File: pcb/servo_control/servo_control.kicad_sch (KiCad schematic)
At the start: 53 parts, among them J1 Jack-DC, J10 Conn_01x03_Female, J11 Conn_01x03_Female, J12 Conn_01x03_Female, J13 Conn_01x03_Female, J14 Conn_01x03_Female, J15 Conn_01x03_Female, J16 Conn_01x03_Female, J17 Conn_01x03_Female, J18 Conn_01x03_Female, J19 Conn_01x03_Female, J2 YLIDAR X4, J20 Conn_01x03_Female, J21 Conn_01x06_Male, J22 GY-87, J3 Conn_01x03_Female, J4 Conn_01x03_Female, J5 Conn_01x03_Female, J6 Conn_01x03_Female, J7 Conn_01x03_Female, J8 Conn_01x03_Female, J9 Conn_01x03_Female, SW1 ESP_PROG, SW2 ESP_RST, U1 PCA9685BS, U2 LM317-3.3_SOT-223, U3 ESP32-WROOM-32, U4 MCP73213-A6SI/MF, U5 PCA9685BS, U6 LM317-5_SOT-223

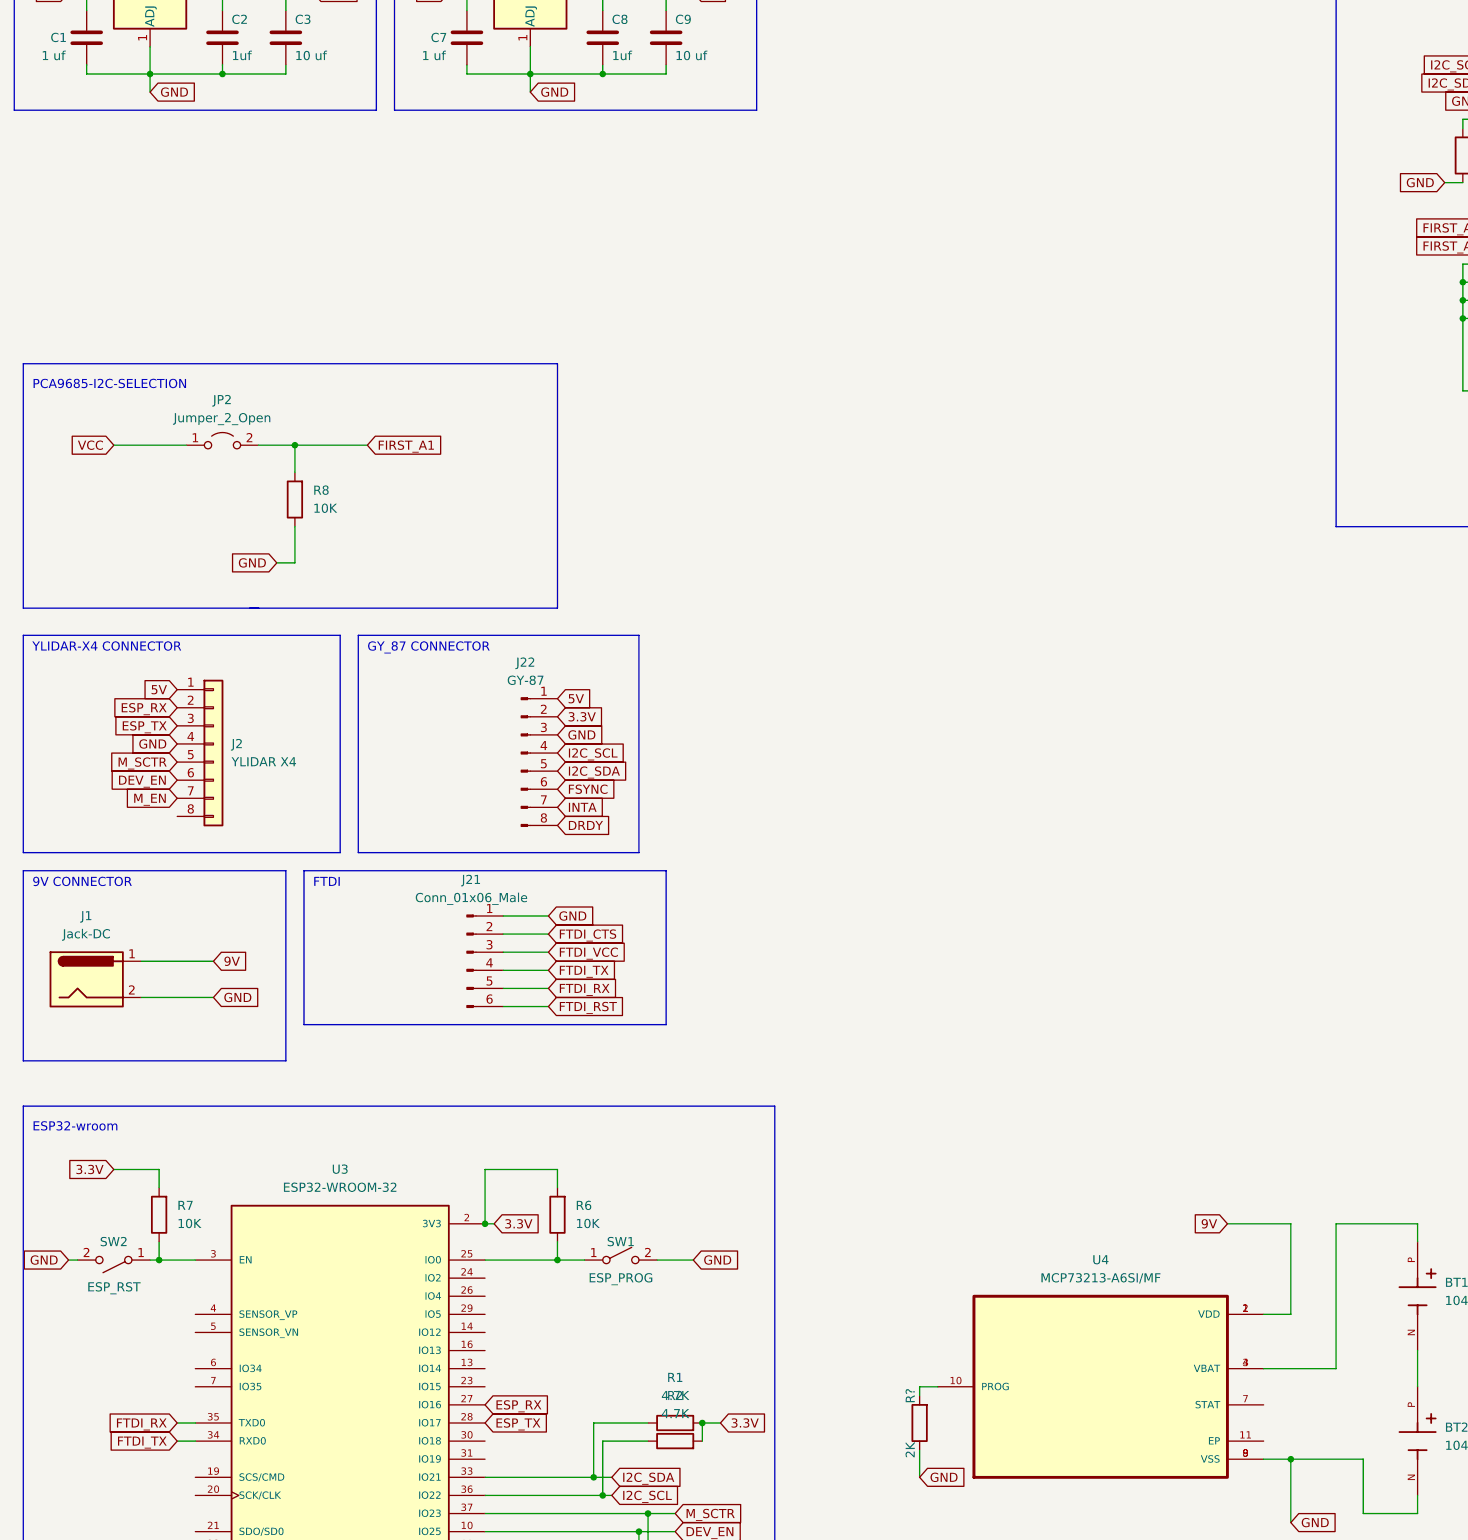
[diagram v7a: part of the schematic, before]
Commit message: add 18650 support + LT1085 regulator
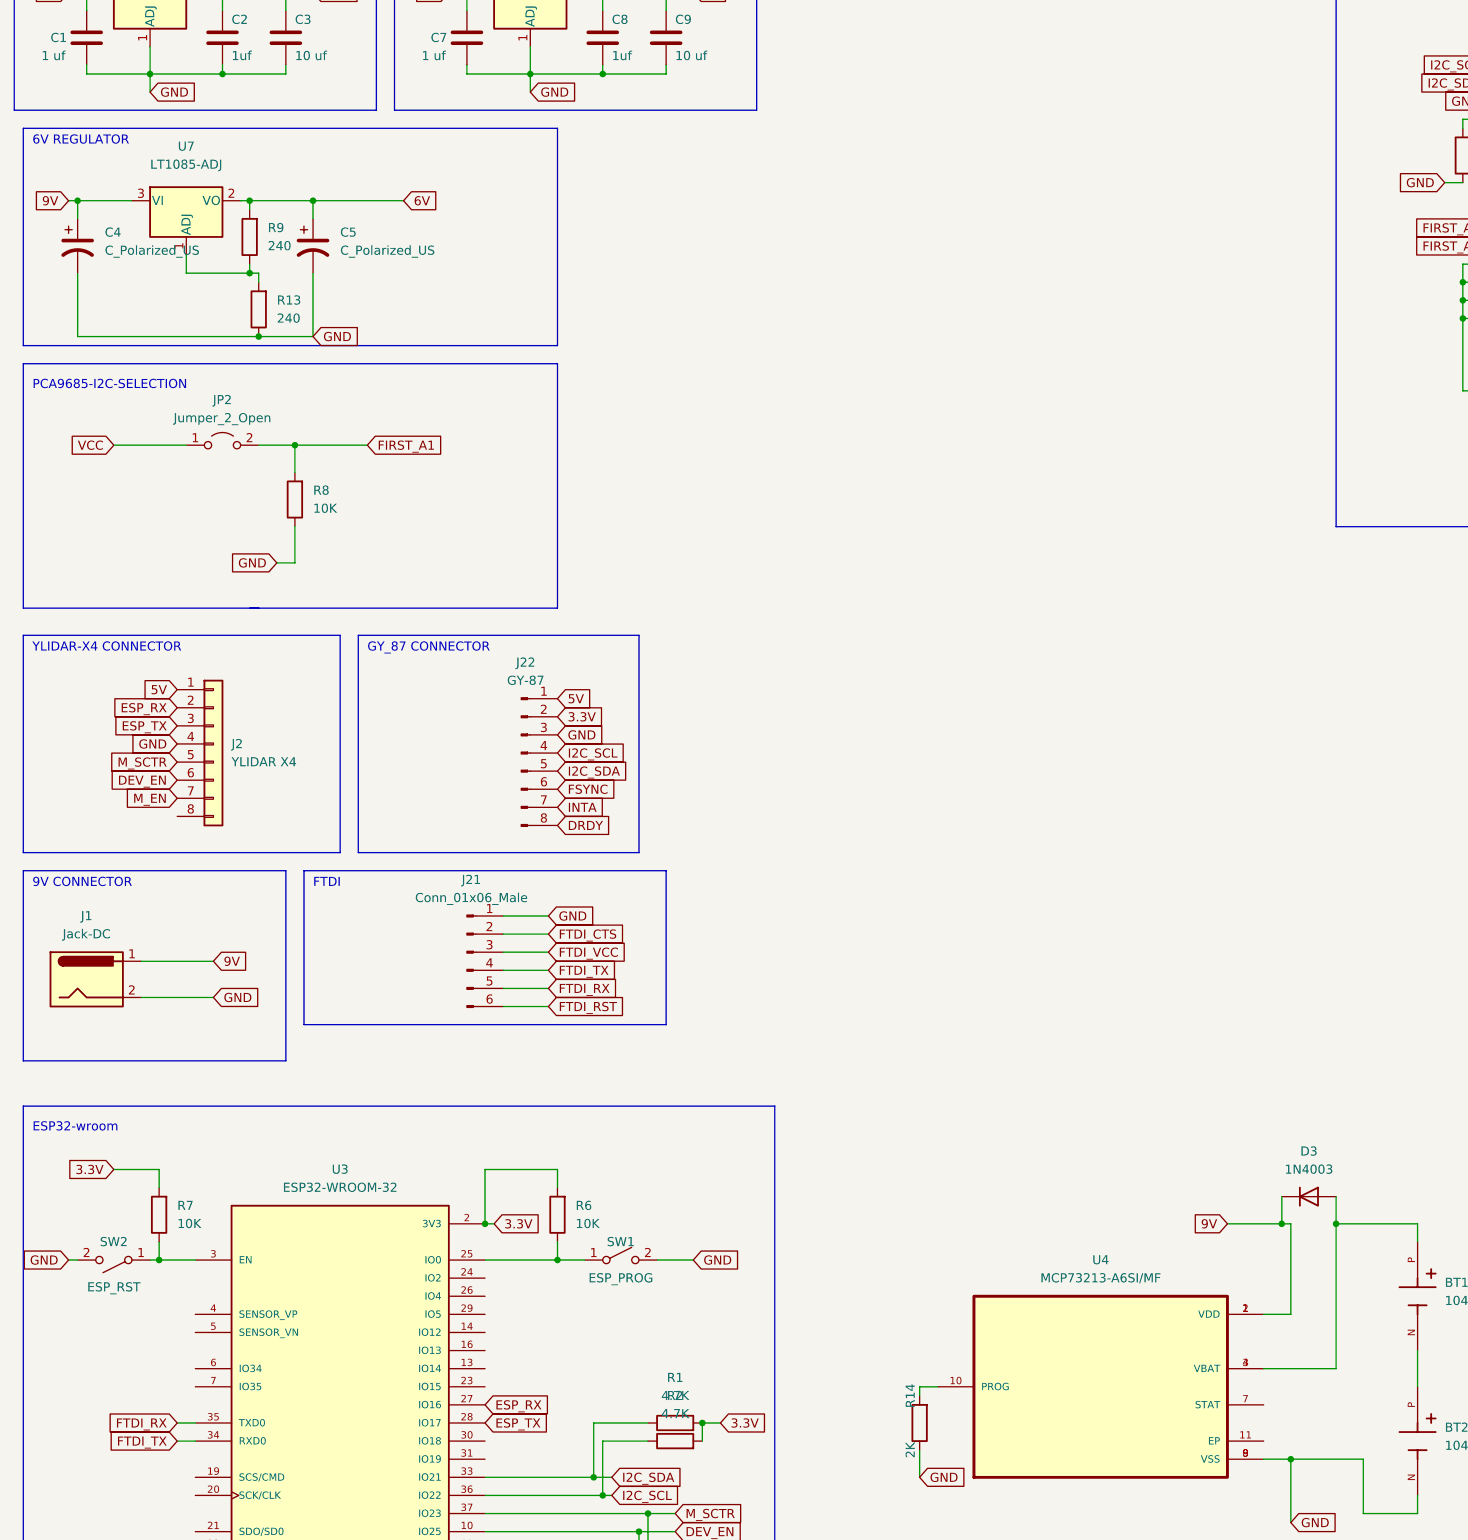
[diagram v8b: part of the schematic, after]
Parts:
- added C4, C5: C_Polarized_US, Capacitor_SMD:CP_Elec_6.3x3, symbol Device:C_Polarized_US
- added D3: 1N4003, Diode_THT:D_DO-41_SOD81_P10.16mm_Horizontal, symbol Diode:1N4003
- added R13, R9: 240, Resistor_SMD:R_0603_1608Metric, symbol Device:R
- added U7: LT1085-ADJ, Package_TO_SOT_THT:TO-247-3_Vertical, symbol Regulator_Linear:LT1085-ADJ
- BT1, BT2: footprint BAT_1043 -> 18650:BAT_1043
- gave numbers to parts that had none: 1
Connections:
- net 9V: now also C4.1, D3.1 (K), U7.3 (VI)
- net GND: now also C4.2, C5.2, R13.1
- net at BT1.P, U4.3 (VBAT), U4.4 (VBAT): now also D3.2 (A)
- new net: R13.2, R9.1, U7.1 (ADJ)
- new net 6V: C5.1, R9.2, U7.2 (VO)
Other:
- note added: "6V REGULATOR"
